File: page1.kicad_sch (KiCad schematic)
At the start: 84 parts

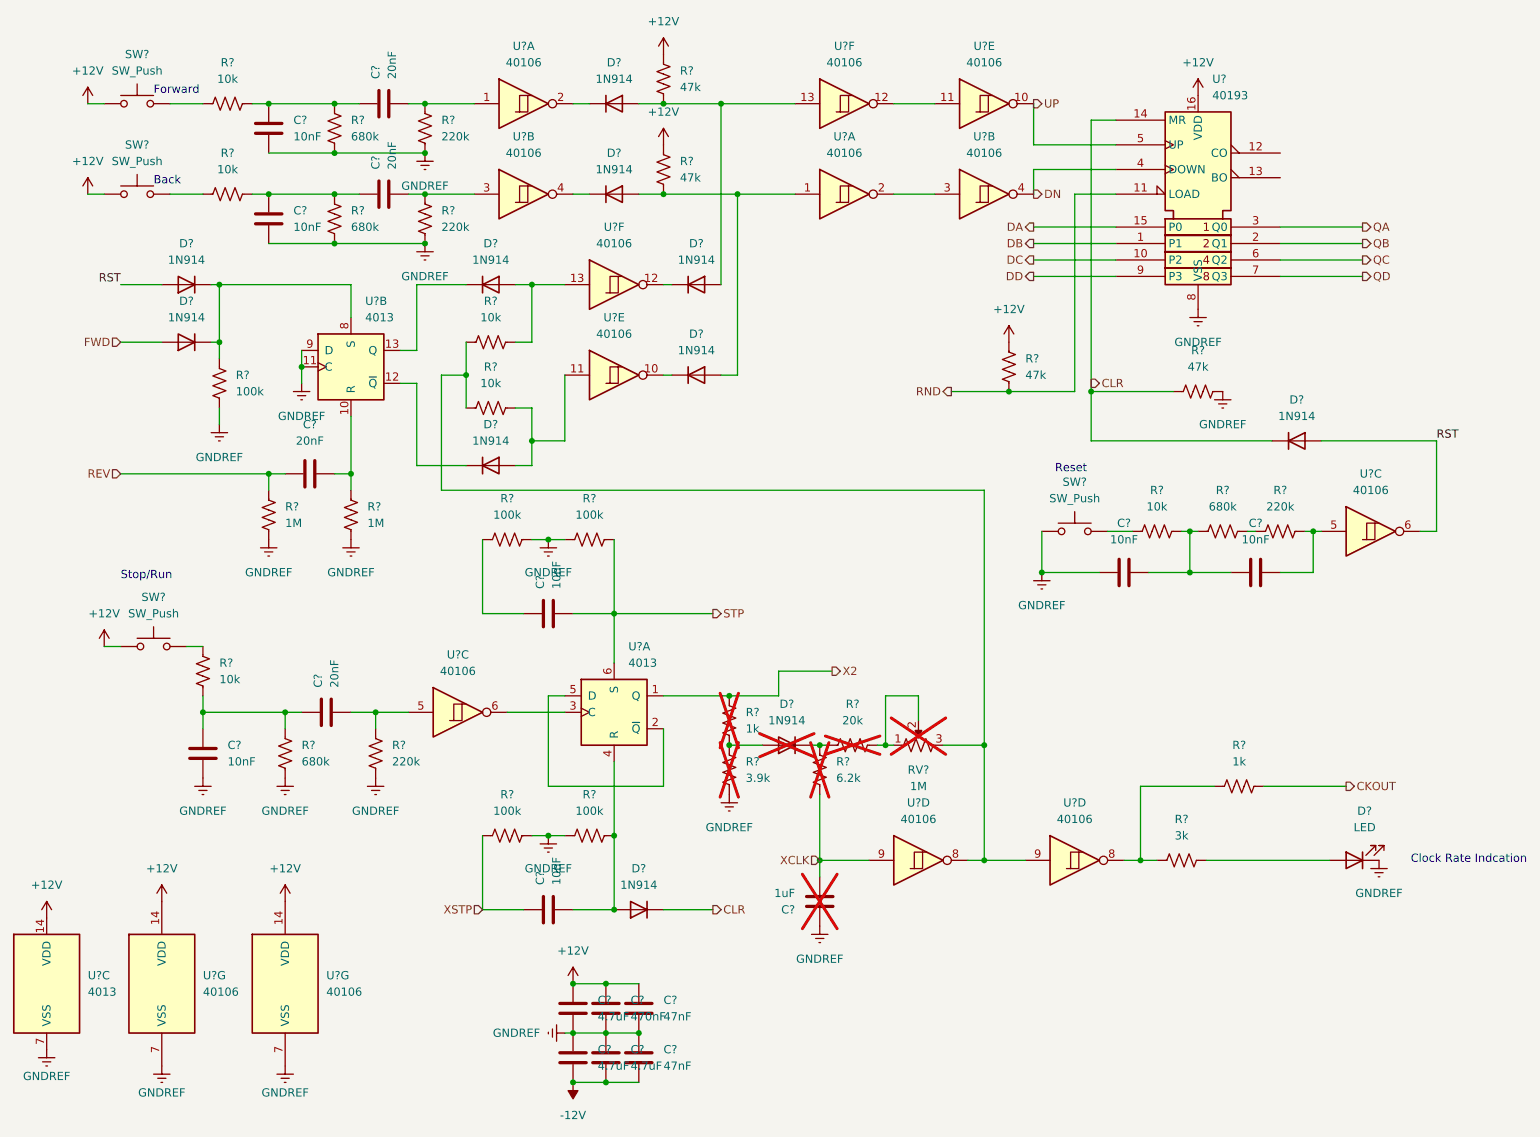
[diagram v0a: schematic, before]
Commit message: created pcb file, placed parts
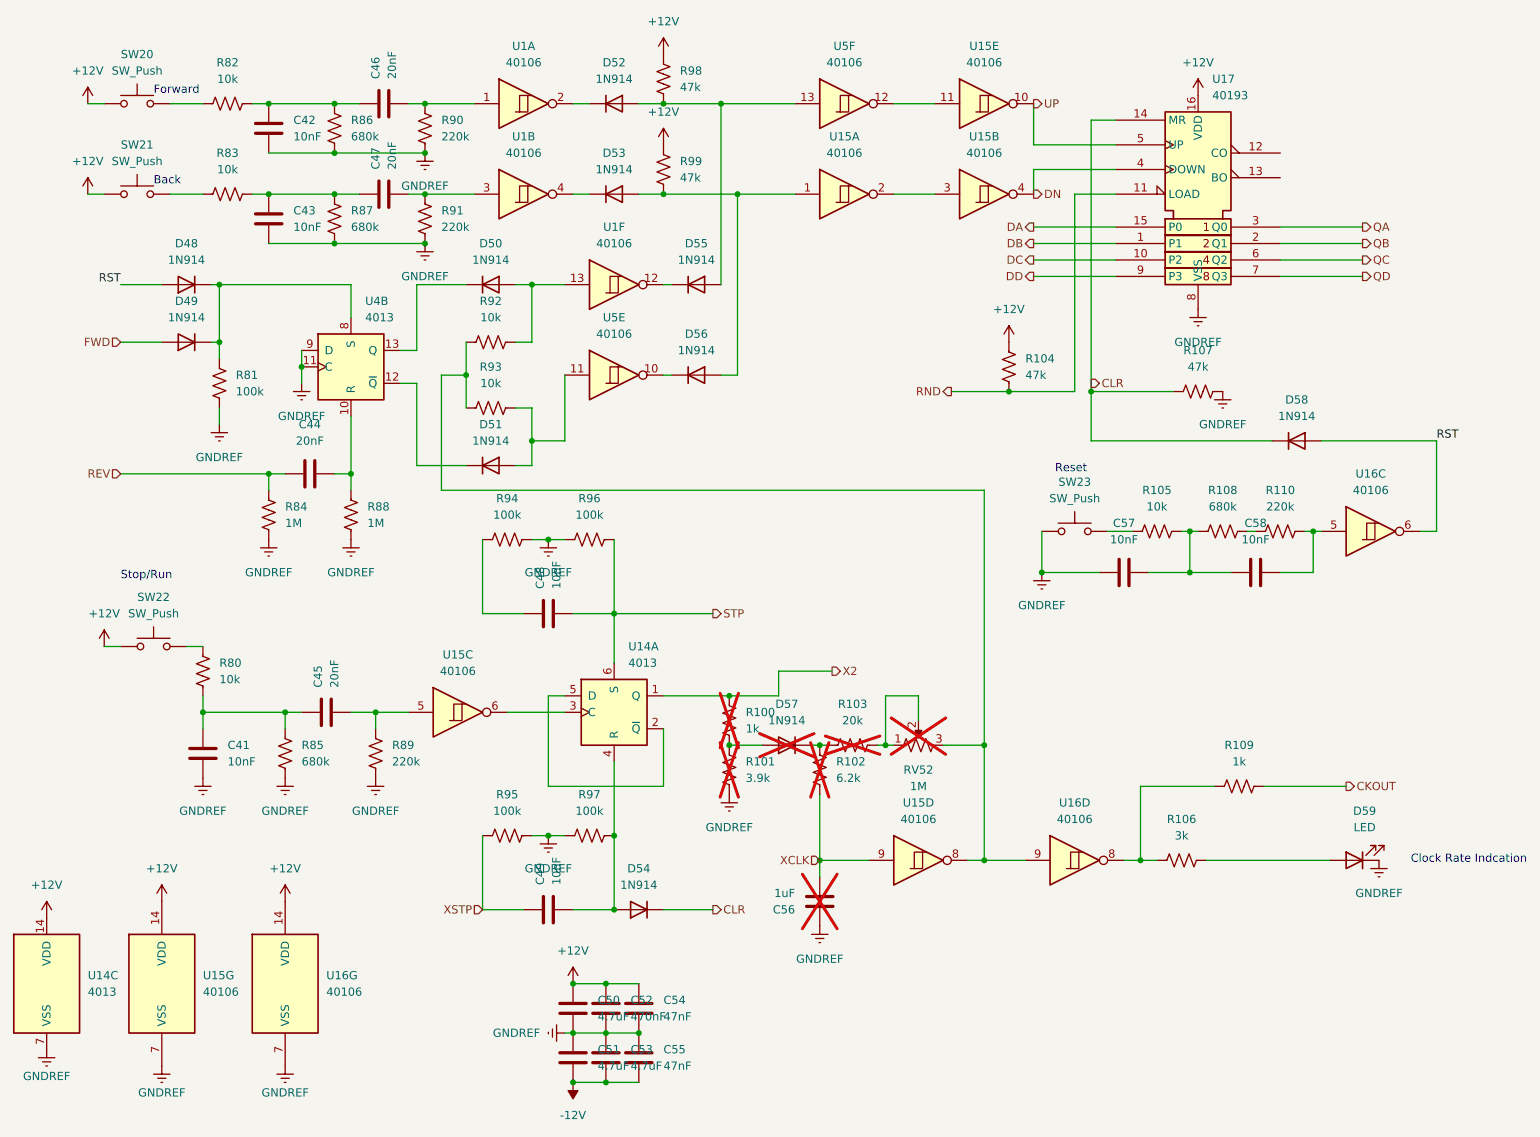
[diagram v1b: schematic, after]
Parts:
- gave numbers to parts that had none: 73

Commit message: init placement/layout
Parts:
- RV52: footprint Potentiometer_THT:Potentiometer_Alps_RK09K_Single_Vertical -> Potentiometer_SMD:Potentiometer_Bourns_TC33X_Vertical
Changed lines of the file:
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@@
       (effects (font (size 1.27 1.27)))
     )
-    (property "Footprint" "Potentiometer_THT:Potentiometer_Alps_RK09K_Single_Vertical" (at 170.18 132.08 0)
+    (property "Footprint" "Potentiometer_SMD:Potentiometer_Bourns_TC33X_Vertical" (at 170.18 132.08 0)
       (effects (font (size 1.27 1.27)) hide)
     )

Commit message: routing and placing
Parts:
- removed C56: 1uF, Capacitor_SMD:C_0805_2012Metric, symbol Device:C
- removed D57: 1N914, Diode_SMD:D_SOD-323F, symbol Device:D
- removed D59: LED, LED_SMD:LED_0805_2012Metric, symbol Device:LED
- removed R100, R109: 1k, Resistor_SMD:R_0603_1608Metric, symbol Device:R_US
- removed R101: 3.9k, Resistor_SMD:R_0603_1608Metric, symbol Device:R_US
- removed R102: 6.2k, Resistor_SMD:R_0603_1608Metric, symbol Device:R_US
- removed R103: 20k, Resistor_SMD:R_0603_1608Metric, symbol Device:R_US
- removed R106: 3k, Resistor_SMD:R_0603_1608Metric, symbol Device:R_US
- removed RV52: 1M, Potentiometer_SMD:Potentiometer_Bourns_TC33X_Vertical, symbol Device:R_Potentiometer_US
- removed unit 5 of U15
- removed unit 4 of U16
- removed unit 6 of U5
- added unit 6 of U1
- renumbered U15 to U1, U4 to U14, U5 to U15, U1 to U15
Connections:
- net XCLK is gone; now on an unnamed net: U15.9
- net UP: now also U1.12
- net at R92.1, R93.1: no longer U15.8
- new net: U1.13, U15.8
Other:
- note added: "Clock Rate Indcation (ON VARICLOCK)"
- note removed: "Clock Rate Indcation"

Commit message: routed 100%
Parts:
- removed C50, C53: 4.7uF, Capacitor_SMD:C_0805_2012Metric, symbol Device:C
- removed C55: 47nF, Capacitor_SMD:C_0603_1608Metric, symbol Device:C
- C51: value 4.7uF -> 470nF
- C54: value 47nF -> 470nF; footprint Capacitor_SMD:C_0603_1608Metric -> Capacitor_SMD:C_0805_2012Metric
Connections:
- net +12V: now also C51.1
- net -12V: no longer C51.2
- net GNDREF: now also C51.2; no longer C51.1
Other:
- moved on the sheet: C52
